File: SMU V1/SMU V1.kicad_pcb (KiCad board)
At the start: 2 copper layers, 42 parts, among them Q1201 SI2301CDS-T1-GE3, U1001 TPS5430DDAR, U1101 AMS1117-3.3, U601 LSM6DSOTR, U801 TPS7A2033PDBVR, U901 TPS7A2033PDBVR

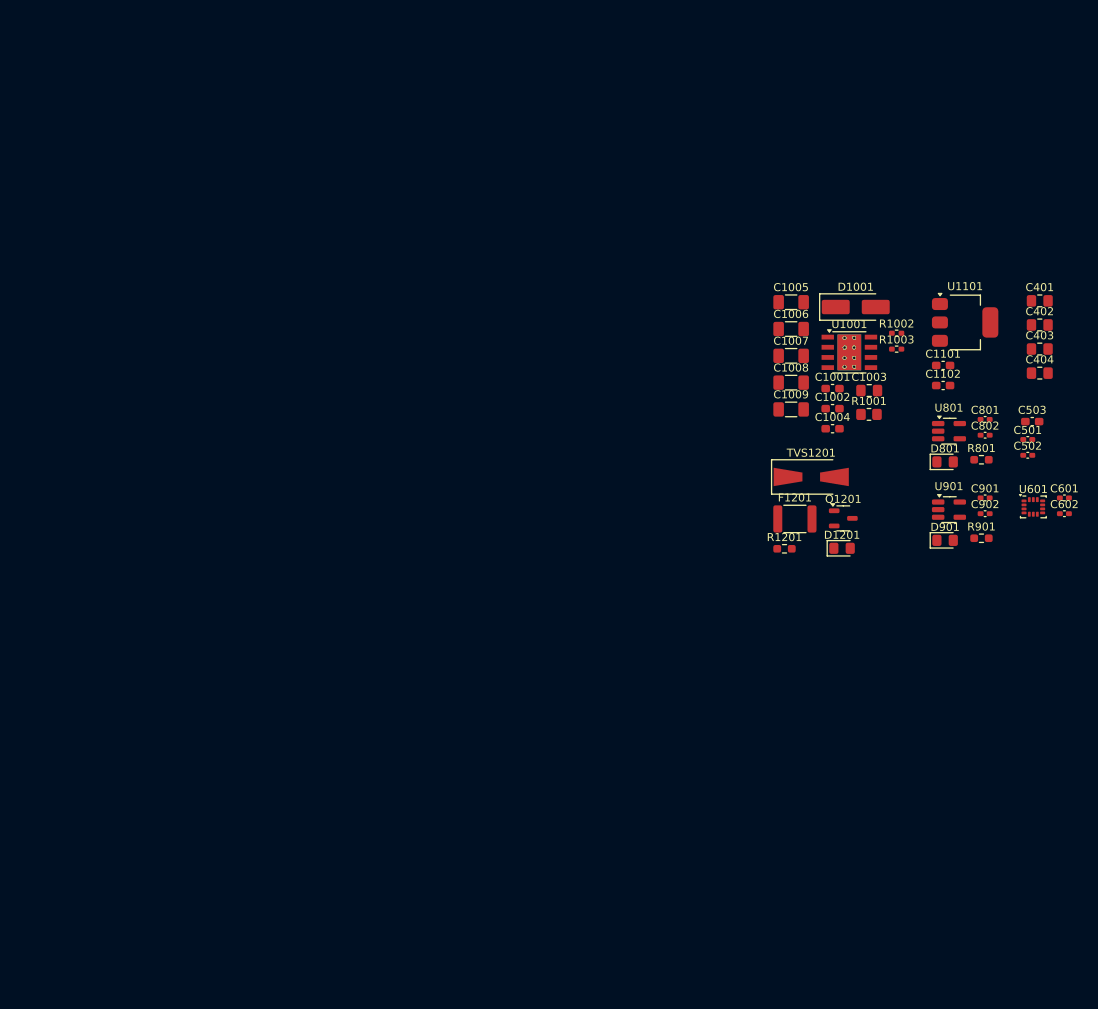
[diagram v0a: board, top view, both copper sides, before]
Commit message: halfway done with routing, still needs antenna
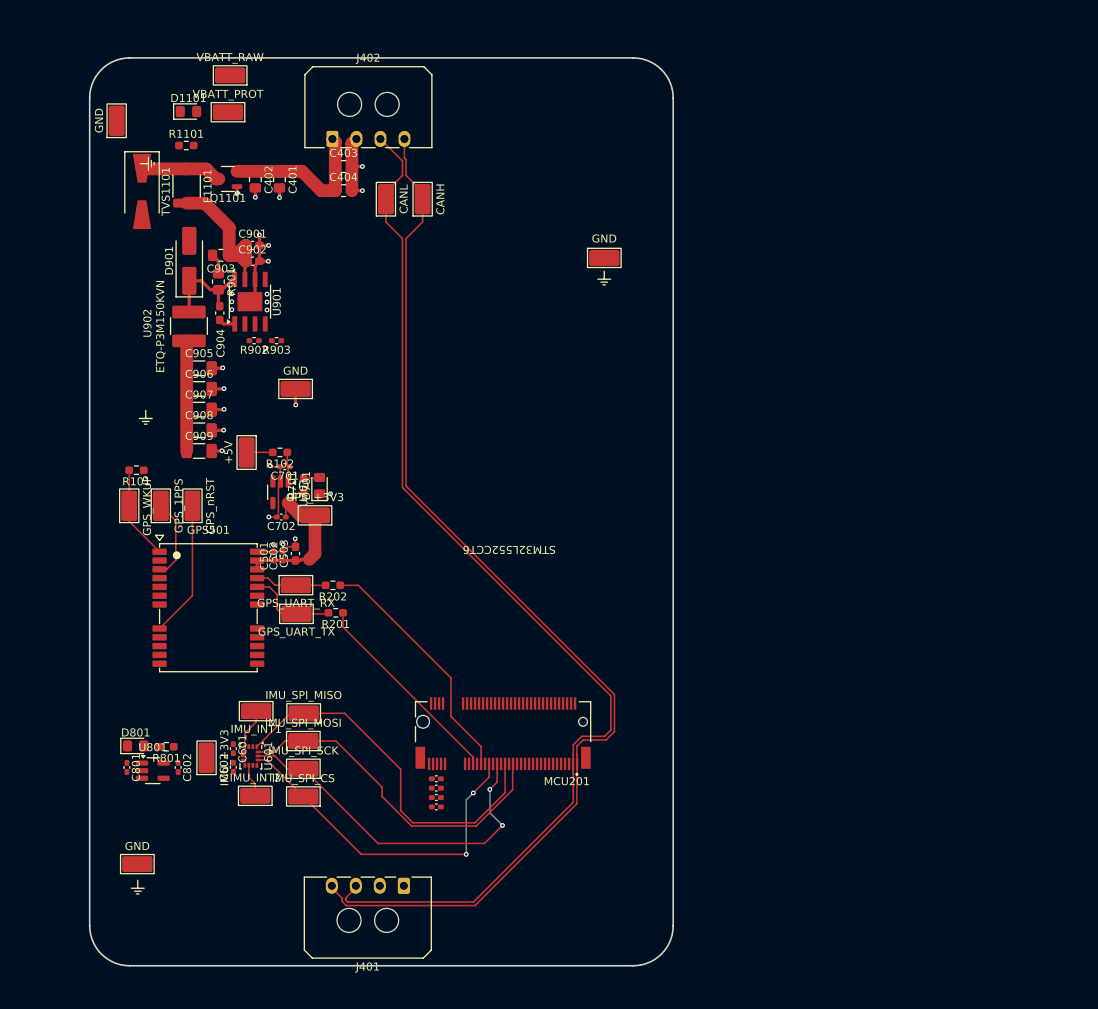
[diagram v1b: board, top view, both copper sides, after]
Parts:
- removed C1001, C1002, C1101, C1102: 22u, Capacitor_SMD:C_0603_1608Metric_Pad1.08x0.95mm_HandSolder
- removed C1003: 1.8p, Capacitor_SMD:C_0805_2012Metric_Pad1.18x1.45mm_HandSolder
- removed C1004: 10n, Capacitor_SMD:C_0603_1608Metric_Pad1.08x0.95mm_HandSolder
- removed C1005, C1006, C1007, C1008, C1009: 100u, Capacitor_SMD:C_1206_3216Metric_Pad1.33x1.80mm_HandSolder
- removed D1001: 550m, Diode_SMD:D_SMA_Handsoldering
- removed D1201: Green, Diode_SMD:D_0805_2012Metric_Pad1.15x1.40mm_HandSolder
- removed F1201: 500mA, Fuse:Fuse_1812_4532Metric
- removed Q1201: SI2301CDS-T1-GE3, Package_TO_SOT_SMD:SOT-23-3
- removed R1001: 180k, Resistor_SMD:R_0805_2012Metric_Pad1.20x1.40mm_HandSolder
- removed R1002: 10k, Resistor_SMD:R_0402_1005Metric_Pad0.72x0.64mm_HandSolder
- removed R1003: 3.3k, Resistor_SMD:R_0402_1005Metric_Pad0.72x0.64mm_HandSolder
- removed R1201: 1.8k, Resistor_SMD:R_0603_1608Metric_Pad0.98x0.95mm_HandSolder
- removed TVS1201: 16Vrwm, Diode_SMD:D_SMA-SMB_Universal_Handsoldering
- removed U1001: TPS5430DDAR, Package_SO:TI_SO-PowerPAD-8_ThermalVias
- removed U1101: AMS1117-3.3, Package_TO_SOT_SMD:SOT-223-3_TabPin2
- added C201: 100n, Capacitor_SMD:C_0402_1005Metric_Pad0.74x0.62mm_HandSolder, F.Cu at (83.0, 129.6)
- added C202: 100n, Capacitor_SMD:C_0402_1005Metric_Pad0.74x0.62mm_HandSolder, F.Cu at (83.0, 128.4)
- added C203: 100n, Capacitor_SMD:C_0402_1005Metric_Pad0.74x0.62mm_HandSolder, F.Cu at (83.0, 127.2)
- added C204: 100n, Capacitor_SMD:C_0402_1005Metric_Pad0.74x0.62mm_HandSolder, F.Cu at (83.0, 126.0)
- added C701: 2.2u, Capacitor_SMD:C_0402_1005Metric_Pad0.74x0.62mm_HandSolder, F.Cu at (64.1, 87.0)
- added C702: 2.2u, Capacitor_SMD:C_0402_1005Metric_Pad0.74x0.62mm_HandSolder, F.Cu at (63.7, 93.3)
- added C903: 1.8p, Capacitor_SMD:C_0805_2012Metric_Pad1.18x1.45mm_HandSolder, F.Cu at (56.1, 60.6)
- added C904: 10n, Capacitor_SMD:C_0603_1608Metric_Pad1.08x0.95mm_HandSolder, F.Cu at (56.0, 67.8)
- added C905: 100u, Capacitor_SMD:C_1206_3216Metric_Pad1.33x1.80mm_HandSolder, F.Cu at (53.4, 74.7)
- added C906: 100u, Capacitor_SMD:C_1206_3216Metric_Pad1.33x1.80mm_HandSolder, F.Cu at (53.4, 77.3)
- added C907: 100u, Capacitor_SMD:C_1206_3216Metric_Pad1.33x1.80mm_HandSolder, F.Cu at (53.4, 79.9)
- added C908: 100u, Capacitor_SMD:C_1206_3216Metric_Pad1.33x1.80mm_HandSolder, F.Cu at (53.4, 82.5)
- added C909: 100u, Capacitor_SMD:C_1206_3216Metric_Pad1.33x1.80mm_HandSolder, F.Cu at (53.4, 85.1)
- added D1101: Green, Diode_SMD:D_0805_2012Metric_Pad1.15x1.40mm_HandSolder, F.Cu at (52.1, 42.6)
- added D701: Green, Diode_SMD:D_0805_2012Metric_Pad1.15x1.40mm_HandSolder, F.Cu at (68.4, 89.4)
- added F1101: 500mA, Fuse:Fuse_1812_4532Metric, F.Cu at (51.8, 51.9)
- added GPS501: LC29HEAMD, bfr_sensors:Quectel LC49, F.Cu at (54.5, 104.7)
- added J401: Connector, Connector_Molex:Molex_Micro-Fit_3.0_43650-0400_1x04_P3.00mm_Horizontal, F.Cu at (79.0, 139.4)
- added J402: Connector, Connector_Molex:Molex_Micro-Fit_3.0_43650-0400_1x04_P3.00mm_Horizontal, F.Cu at (70.0, 46.1)
- added MCU201: Krill, bfr_connectors:TE_1-2199119-5, F.Cu at (91.4, 120.4)
- added Q1101: SI2301CDS-T1-GE3, Package_TO_SOT_SMD:SOT-23-3, F.Cu at (57.0, 51.1)
- added R101: 0, Resistor_SMD:R_0603_1608Metric_Pad0.98x0.95mm_HandSolder, F.Cu at (45.6, 87.5)
- added R102: 0, Resistor_SMD:R_0603_1608Metric_Pad0.98x0.95mm_HandSolder, F.Cu at (63.5, 85.2)
- added R1101: 1.8k, Resistor_SMD:R_0603_1608Metric_Pad0.98x0.95mm_HandSolder, F.Cu at (51.8, 46.9)
- added R201: 0, Resistor_SMD:R_0603_1608Metric_Pad0.98x0.95mm_HandSolder, F.Cu at (70.5, 105.3)
- added R202: 0, Resistor_SMD:R_0603_1608Metric_Pad0.98x0.95mm_HandSolder, F.Cu at (70.1, 101.9)
- added R701: 120, Resistor_SMD:R_0603_1608Metric_Pad0.98x0.95mm_HandSolder, F.Cu at (66.5, 89.4)
- added R902: 10k, Resistor_SMD:R_0402_1005Metric_Pad0.72x0.64mm_HandSolder, F.Cu at (60.3, 71.3)
- added R903: 3.3k, Resistor_SMD:R_0402_1005Metric_Pad0.72x0.64mm_HandSolder, F.Cu at (63.1, 71.3)
- added TP205: CANH, bfr_utilities:TestPoint_Keystone_5019_Miniature, F.Cu at (81.3, 53.6)
- added TP206: CANL, bfr_utilities:TestPoint_Keystone_5019_Miniature, F.Cu at (76.7, 53.6)
- added TP301: VBATT_RAW, bfr_utilities:TestPoint_Keystone_5019_Miniature, F.Cu at (57.3, 38.1)
- added TP302: VBATT_PROT, bfr_utilities:TestPoint_Keystone_5019_Miniature, F.Cu at (57.0, 42.7)
- added TP303: +5V, bfr_utilities:TestPoint_Keystone_5019_Miniature, F.Cu at (59.3, 85.3)
- added TP305: GND, bfr_utilities:TestPoint_Keystone_5019_Miniature, F.Cu at (45.7, 136.7)
- added TP306: GND, bfr_utilities:TestPoint_Keystone_5019_Miniature, F.Cu at (104.0, 60.9)
- added TP307: GND, bfr_utilities:TestPoint_Keystone_5019_Miniature, F.Cu at (43.1, 43.8)
- added TP308: GND, bfr_utilities:TestPoint_Keystone_5019_Miniature, F.Cu at (65.5, 77.3)
- added TP501: GPS_UART_RX, bfr_utilities:TestPoint_Keystone_5019_Miniature, F.Cu at (65.5, 101.8)
- added TP502: GPS_UART_TX, bfr_utilities:TestPoint_Keystone_5019_Miniature, F.Cu at (65.6, 105.4)
- added TP503: GPS_WKUP, bfr_utilities:TestPoint_Keystone_5019_Miniature, F.Cu at (44.7, 91.9)
- added TP504: GPS_1PPS, bfr_utilities:TestPoint_Keystone_5019_Miniature, F.Cu at (48.6, 91.9)
- added TP505: GPS_nRST, bfr_utilities:TestPoint_Keystone_5019_Miniature, F.Cu at (52.6, 91.9)
- added TP506: GPS_+3V3, bfr_utilities:TestPoint_Keystone_5019_Miniature, F.Cu at (67.9, 93.1)
- added TP601: IMU_+3V3, bfr_utilities:TestPoint_Keystone_5019_Miniature, F.Cu at (54.3, 123.4)
- added TP602: IMU_INT2, bfr_utilities:TestPoint_Keystone_5019_Miniature, F.Cu at (60.4, 128.2)
- added TP603: IMU_INT1, bfr_utilities:TestPoint_Keystone_5019_Miniature, F.Cu at (60.5, 117.6)
- added TP604: IMU_SPI_CS, bfr_utilities:TestPoint_Keystone_5019_Miniature, F.Cu at (66.4, 128.2)
- added TP605: IMU_SPI_MISO, bfr_utilities:TestPoint_Keystone_5019_Miniature, F.Cu at (66.5, 117.9)
- added TP606: IMU_SPI_MOSI, bfr_utilities:TestPoint_Keystone_5019_Miniature, F.Cu at (66.4, 121.3)
- added TP607: IMU_SPI_SCK, bfr_utilities:TestPoint_Keystone_5019_Miniature, F.Cu at (66.4, 124.8)
- added TVS1101: 16Vrwm, Diode_SMD:D_SMA-SMB_Universal_Handsoldering, F.Cu at (46.2, 52.6)
- added U701: TPS7A2033PDBVR, Package_TO_SOT_SMD:SOT-23-5_HandSoldering, F.Cu at (63.6, 90.2)
- added U902: ETQ-P3M150KVN, bfr_inductors:BWVS005050404R7M00, F.Cu at (52.1, 69.5)
- C901, C902: value 2.2u -> 22u; footprint Capacitor_SMD:C_0402_1005Metric_Pad0.74x0.62mm_HandSolder -> Capacitor_SMD:C_0603_1608Metric_Pad1.08x0.95mm_HandSolder
- D901: value Green -> 550m; footprint Diode_SMD:D_0805_2012Metric_Pad1.15x1.40mm_HandSolder -> Diode_SMD:D_SMA_Handsoldering
- R901: value 120 -> 180k; footprint Resistor_SMD:R_0603_1608Metric_Pad0.98x0.95mm_HandSolder -> Resistor_SMD:R_0805_2012Metric_Pad1.20x1.40mm_HandSolder
- U901: value TPS7A2033PDBVR -> TPS5430DDAR; footprint Package_TO_SOT_SMD:SOT-23-5_HandSoldering -> Package_SO:TI_SO-PowerPAD-8
- moved C801 115.8 mm to (44.4, 124.6), turned to -90 degrees
- moved C802 109.1 mm to (50.8, 124.6), turned to -90 degrees
- moved C602 108.6 mm to (57.7, 124.6), turned to 90 degrees
- moved C601 108.5 mm to (57.7, 122.3), turned to -90 degrees
- moved U801 108.2 mm to (47.6, 125.0)
- moved R801 108.0 mm to (49.3, 122.0), turned to 180 degrees
- moved D801 107.2 mm to (45.5, 121.9)
- moved U601 102.6 mm to (59.9, 123.2), turned to -90 degrees
- moved D901 100.7 mm to (52.2, 61.3), turned to 90 degrees
- moved R901 100.6 mm to (55.8, 63.9), turned to -90 degrees
- moved C402 99.7 mm to (60.4, 51.1), turned to -90 degrees
- moved C901 96.9 mm to (60.1, 59.4)
- moved C902 96.9 mm to (60.1, 61.3)
- moved C401 96.2 mm to (63.4, 51.1), turned to -90 degrees
- moved C501 95.4 mm to (62.7, 98.2), turned to 90 degrees
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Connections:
- C802 pad 1: /GPS/PP3300_GPS_VCC -> /IMU/PP3300_IMU_VDD
- C901 pad 1: +5V -> /Power/5V Buck/PPVAR_VBATT_PROT
- C902 pad 1: /IMU/PP3300_IMU_VDD -> /Power/5V Buck/PPVAR_VBATT_PROT
- D901 pad 1: GND -> /Power/5V Buck/SWITCH_NODE
- D901 pad 2: Net-(D901-A) -> GND
- R801 pad 1: /GPS/PP3300_GPS_VCC -> /IMU/PP3300_IMU_VDD
- R901 pad 1: /IMU/PP3300_IMU_VDD -> /Power/5V Buck/Rsnub
- R901 pad 2: Net-(D901-A) -> /Power/5V Buck/SWITCH_NODE
- U801 pad 3: /GPS/GPS_LDO_EN -> /IMU/GPS Power/LDO_EN
- U801 pad 5: /GPS/PP3300_GPS_VCC -> /IMU/PP3300_IMU_VDD
- U901 pad 1: +5V -> Net-(U901-BOOT)
- U901 pad 2: GND -> unconnected-(U901-NC-Pad2)
- U901 pad 3: /IMU/GPS Power/LDO_EN -> unconnected-(U901-NC-Pad3)
- U901 pad 4: unconnected-(U901-NC-Pad4) -> /Power/5V Buck/BUCK_VSENSE
- U901 pad 5: /IMU/PP3300_IMU_VDD -> unconnected-(U901-EN-Pad5)
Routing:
- net /CAN+: track 0.00 -> 136.6 mm
- net /CAN-: track 0.00 -> 136.2 mm
- net GND: track 0.00 -> 50.2 mm, vias 0 -> 20
- net /IMU_SPI.MISO: track 0.00 -> 46.6 mm
- net /IMU_SPI.SCK: track 0.00 -> 44.7 mm, vias 0 -> 2
- net /IMU_SPI.CS: track 0.00 -> 43.4 mm, vias 0 -> 2
- net /IMU_SPI.MOSI: track 0.00 -> 42.6 mm
- net Net-(MCU201A-PA1): track 0.00 -> 31.0 mm
- net Net-(MCU201A-PA0): track 0.00 -> 25.6 mm
- net /GPS/PP3300_GPS_VCC: track 0.00 -> 21.8 mm
- net /Main IO/VBATT+: track 0.00 -> 19.9 mm
- net /Power/5V Buck/PPVAR_VBATT_PROT: track 0.00 -> 19.3 mm
- net +5V: track 0.00 -> 17.1 mm
- net /GPS/GPS_nRST: track 0.00 -> 17.0 mm
- net /Power/5V Buck/SWITCH_NODE: track 0.00 -> 12.7 mm
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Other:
- board outline added: 72.9 x 113.5 mm
- copper layers 2 -> 4

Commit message: finished, should prob double check the high frequency stuff
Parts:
- removed R101: 0, Resistor_SMD:R_0603_1608Metric_Pad0.98x0.95mm_HandSolder
- added C1001: 100p, Capacitor_SMD:C_0402_1005Metric_Pad0.74x0.62mm_HandSolder, F.Cu at (48.8, 110.1)
- added C1002: 100n, Capacitor_SMD:C_0402_1005Metric_Pad0.74x0.62mm_HandSolder, F.Cu at (41.8, 116.1)
- added C1003: 100p, Capacitor_SMD:C_0402_1005Metric_Pad0.74x0.62mm_HandSolder, F.Cu at (41.8, 117.4)
- added C1004: 100p, Capacitor_SMD:C_0402_1005Metric_Pad0.74x0.62mm_HandSolder, F.Cu at (47.7, 114.2)
- added C1005: 100p, Capacitor_SMD:C_0402_1005Metric_Pad0.74x0.62mm_HandSolder, F.Cu at (47.1, 116.3)
- added J1001: SMA, bfr_connectors:THT SMA, F.Cu at (47.1, 122.5)
- added L1001: 68n, Inductor_SMD:L_0402_1005Metric_Pad0.77x0.64mm_HandSolder, F.Cu at (41.7, 121.9)
- added R1001: 10, Resistor_SMD:R_0402_1005Metric_Pad0.72x0.64mm_HandSolder, F.Cu at (42.2, 113.2)
- added R1002: 0, Resistor_SMD:R_0402_1005Metric_Pad0.72x0.64mm_HandSolder, F.Cu at (47.9, 112.3)
- D1101: value Green -> Vbatt PGOOD
- D701, D801: value Green -> GPS Power
- moved C801 14.4 mm to (55.7, 133.4), turned to 0 degrees
- moved D801 12.8 mm to (53.0, 132.3), turned to 90 degrees
- moved TP303 12.7 mm to (47.0, 81.9)
- moved U801 9.95 mm to (56.1, 130.2), turned to 90 degrees
- moved R801 7.47 mm to (53.1, 128.4), turned to -90 degrees
- moved C802 5.49 mm to (55.7, 127.0), turned to 0 degrees
- moved TP306 4.27 mm to (101.4, 57.6)
- moved TP302 3.91 mm to (60.1, 45.1)
- moved TP307 3.76 mm to (46.7, 42.8)
- moved TP301 3.24 mm to (60.0, 39.8)
- moved C502 3.07 mm to (66.9, 98.0)
- moved C702 3.07 mm to (66.7, 93.2)
- moved C503 3.07 mm to (68.5, 97.7)
- moved GPS501 3.07 mm to (57.6, 104.5)
- moved R701 3.07 mm to (69.5, 89.2)
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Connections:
- GPS501 pad 11: /GPS/GPS_ANTENNA -> /Antenna/GPS_ANT_RF
- GPS501 pad 9: /GPS/GPS_VDD_RF -> /Antenna/GPS_RF_VDD
- MCU201 pad 44: /GPS/GPS_ANT_ON -> /Microcontroller/GPS_MODE
- MCU201 pad 48: /Microcontroller/GPS_WKUP -> unconnected-(MCU201B-PB1-Pad48)
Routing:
- net /GPS/GPS_1PPS: track 10.1 -> 54.3 mm, vias 0 -> 2
- net GND: track 50.2 -> 73.2 mm, vias 20 -> 165
- net /Power/5V Buck/PPVAR_VBATT_PROT: track 19.3 -> 41.3 mm, vias 0 -> 3
- net +5V: track 17.1 -> 39.0 mm, vias 0 -> 21
- net /IMU/PP3300_IMU_VDD: track 0.00 -> 19.6 mm
- net /Main IO/VBATT+: track 19.9 -> 32.5 mm
- net /Antenna/GPS_RF_VDD: track 0.00 -> 11.7 mm
- net /Antenna/ANT_OUT_RF: track 0.00 -> 10.7 mm
- net /Antenna/GPS_RF_VDD_R: track 0.00 -> 7.96 mm
- net /GPS/GPS_WKUP: track 11.8 -> 7.31 mm
- net /Antenna/GPS_ANT_RF: track 0.00 -> 4.16 mm
- net /Power/5V Buck/BUCK_VSENSE: track 0.00 -> 4.04 mm
- net /Antenna/GPS_ANT_RF_R: track 0.00 -> 3.03 mm
- net /GPS/GPS_UART.TX: track 11.4 -> 8.49 mm
- net Net-(D1101-A): track 0.00 -> 2.43 mm
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- added copper zone on F.Cu, net +5V
- added copper zone on In2.Cu, net +5V
- added copper zone on B.Cu, net /Main IO/VBATT+
- added copper zone on B.Cu, net GND
- added copper zone on F.Cu, net GND
- added copper zone on In1.Cu, net GND
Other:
- board text added: "GPS Power"
- board text added: "IMU Power"
